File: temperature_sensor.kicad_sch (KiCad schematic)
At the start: 13 parts, among them U3 XIAO-SAMD21-SMD, U5 TMP37FT9Z

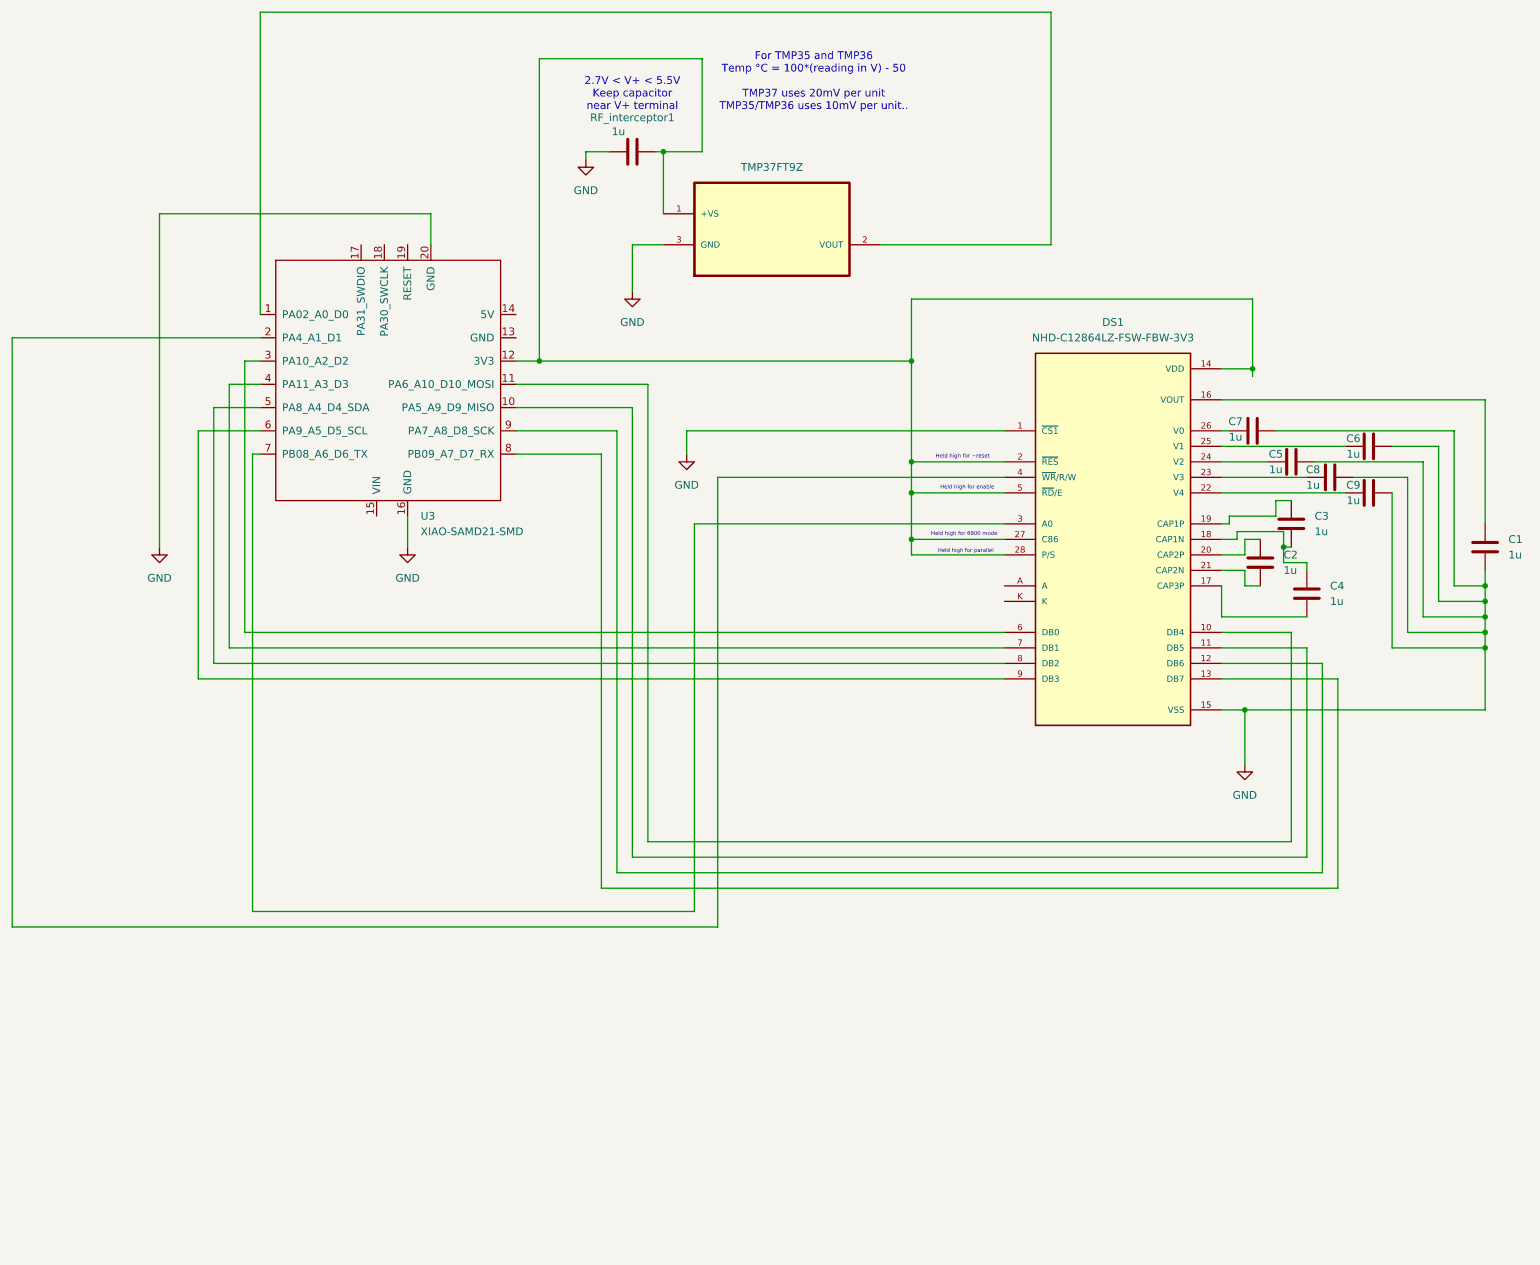
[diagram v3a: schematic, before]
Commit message: added potentiometer, photoresistor, switch between the two and off, and added a F/C switch. need to up current into LCD's A pin
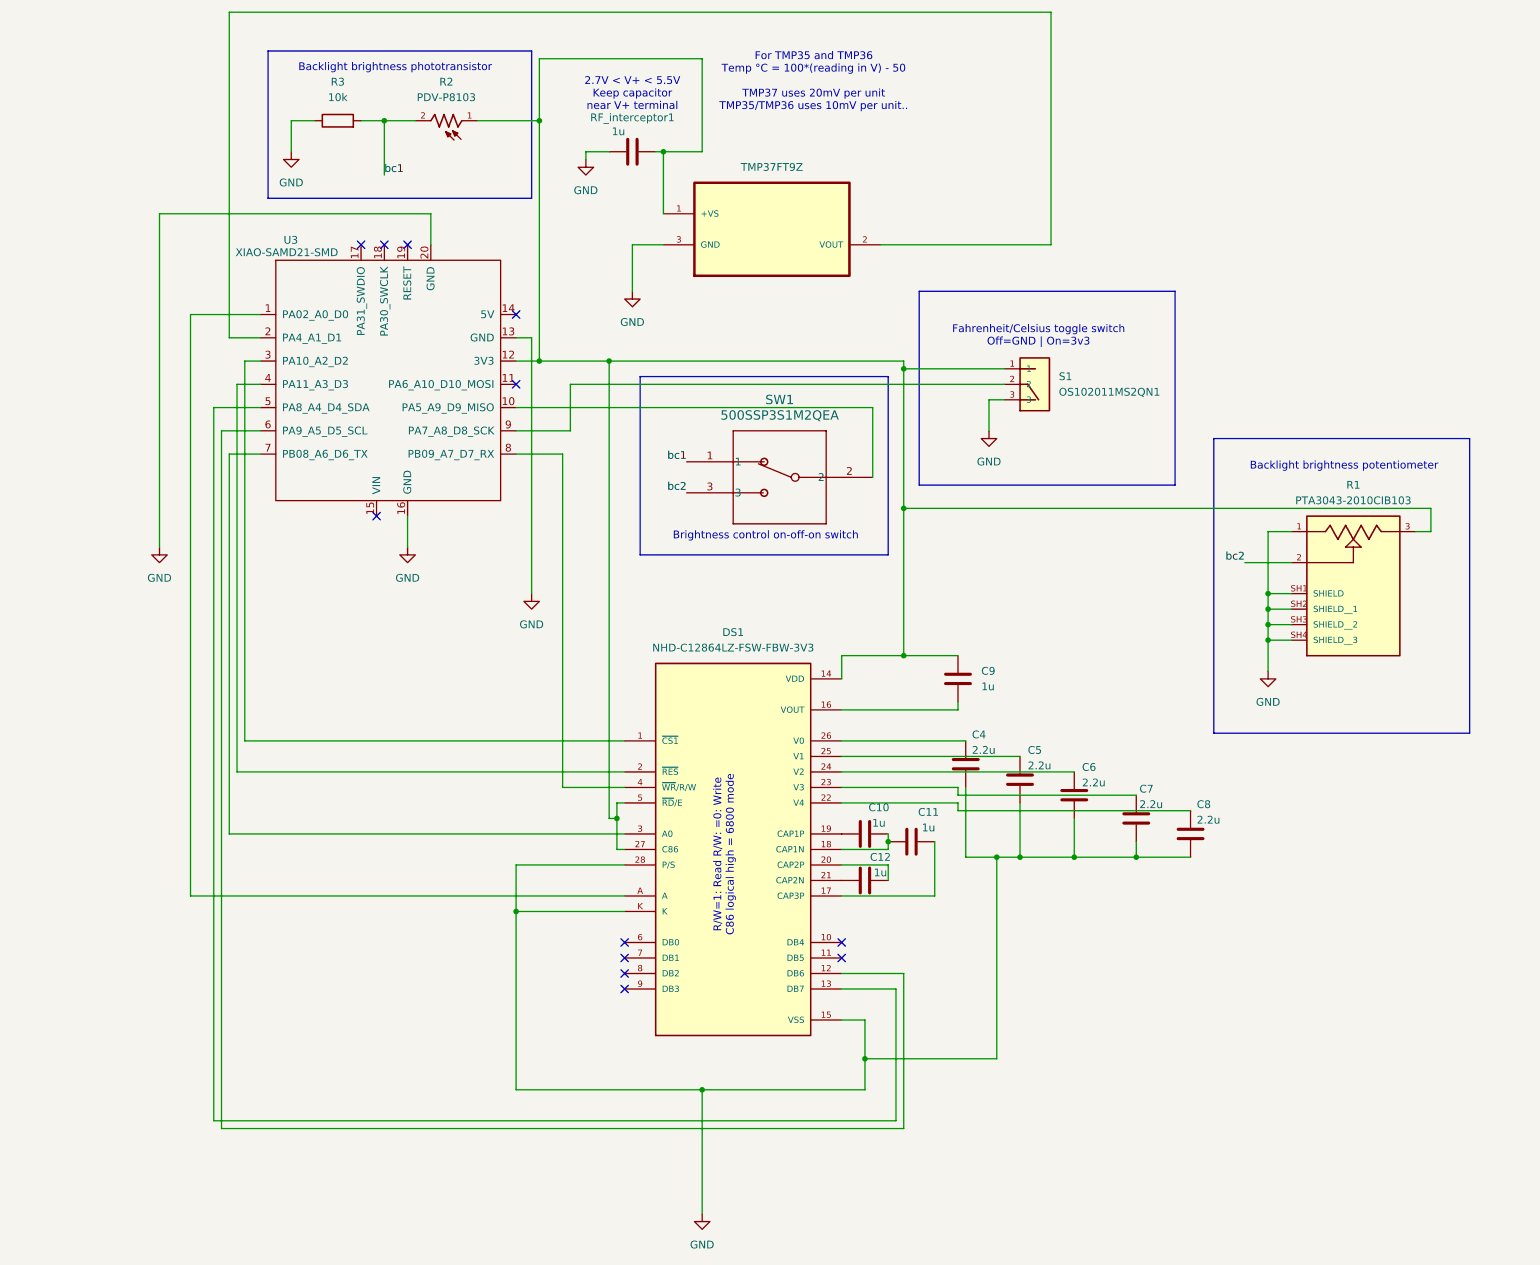
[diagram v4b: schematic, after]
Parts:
- removed C1, C2, C3: 1u, symbol Device:C
- added C10, C11, C12: 1u, symbol Device:C
- added R1: PTA3043-2010CIB103, PTA3043-2010CIB103:TRIM_PTA3043-2010CIB103, symbol PTA3043-2010CIB103:PTA3043-2010CIB103
- added R2: PDV-P8103, PDV-P8103:PHODET_PDV-P8103, symbol PDV-P8103:PDV-P8103
- added R3: 10k, symbol Device:R
- added S1: OS102011MS2QN1, OS102011MS2QN1:SW_OS102011MS2QN1, symbol OS102011MS2QN1:OS102011MS2QN1
- added SW1: 500SSP3S1M2QEA, TO_1M2QEA_EWI, symbol OnOffOn500SSP3S1M2QEA:500SSP3S1M2QEA
- C4, C5, C6, C7, C8: value 1u -> 2.2u
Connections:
- net GND: now also C4.1, C5.1, C6.1, C7.1, C8.1, DS1.28 (P/S), DS1.K, U3.13 (GND), R1.1, R1.SH1 (SHIELD), R1.SH2 (SHIELD__1), R1.SH3 (SHIELD__2), R1.SH4 (SHIELD__3), R3.1, S1.3; no longer C5.2, C6.2, C7.2, C8.2, C9.2, DS1.1 (~{CS1})
- net at C9.1: now also DS1.16 (VOUT); no longer DS1.22 (V4)
- net at DS1.26 (V0): now also C4.2; no longer C7.1
- net at DS1.14 (VDD), DS1.27 (C86), DS1.5 (~{RD}/E)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: now also C9.2, R1.3, R2.1, S1.1; no longer DS1.2 (~{RES}), DS1.28 (P/S)
- net at DS1.20 (CAP2P): now also C12.2
- net at DS1.21 (CAP2N): now also C12.1
- net at DS1.10 (DB4): no longer U3.11 (PA6_A10_D10_MOSI)
- net at U3.10 (PA5_A9_D9_MISO): now also SW1.2; no longer DS1.11 (DB5)
- net at DS1.12 (DB6): now also U3.6 (PA9_A5_D5_SCL); no longer U3.9 (PA7_A8_D8_SCK)
- net at DS1.13 (DB7): now also U3.5 (PA8_A4_D4_SDA); no longer U3.8 (PB09_A7_D7_RX)
- net at DS1.17 (CAP3P): now also C11.2; no longer C4.2
- net at DS1.18 (CAP1N): now also C10.2, C11.1; no longer C4.1
- net at DS1.19 (CAP1P): now also C10.1
- net at DS1.23 (V3): now also C7.2; no longer C8.1
- net at DS1.24 (V2): now also C6.2; no longer C5.1
- net at DS1.25 (V1): now also C5.2; no longer C6.1
- net at DS1.4 (~{WR}/R/W): now also U3.8 (PB09_A7_D7_RX); no longer U3.2 (PA4_A1_D1)
- net at U3.3 (PA10_A2_D2): now also DS1.1 (~{CS1}); no longer DS1.6 (DB0)
- net at U3.4 (PA11_A3_D3): now also DS1.2 (~{RES}); no longer DS1.7 (DB1)
- net at DS1.8 (DB2): no longer U3.5 (PA8_A4_D4_SDA)
- net at DS1.9 (DB3): no longer U3.6 (PA9_A5_D5_SCL)
- net at DS1.A: now also U3.1 (PA02_A0_D0)
- net at U5.2 (VOUT): now also U3.2 (PA4_A1_D1); no longer U3.1 (PA02_A0_D0)
- new net: C8.2, DS1.22 (V4)
- new net: S1.2, U3.9 (PA7_A8_D8_SCK)
- new net bc1: R2.2, R3.2, SW1.1
- new net bc2: R1.2, SW1.3
- no-connect marks 0 -> 12
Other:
- note added: "Backlight brightness phototransistor"
- note added: "Backlight brightness potentiometer"
- note added: "Brightness control on-off-on switch"
- note added: "Fahrenheit/Celsius toggle switch Off=GND | On=3v3"
- note added: "R/W=1: Read R/W: =0: Write C86 logical high = 6800 mode"
- note removed: "Held high for 6800 mode"
- note removed: "Held high for enable"
- note removed: "Held high for parallel"
- note removed: "Held high for ~reset"
- moved on the sheet: DS1

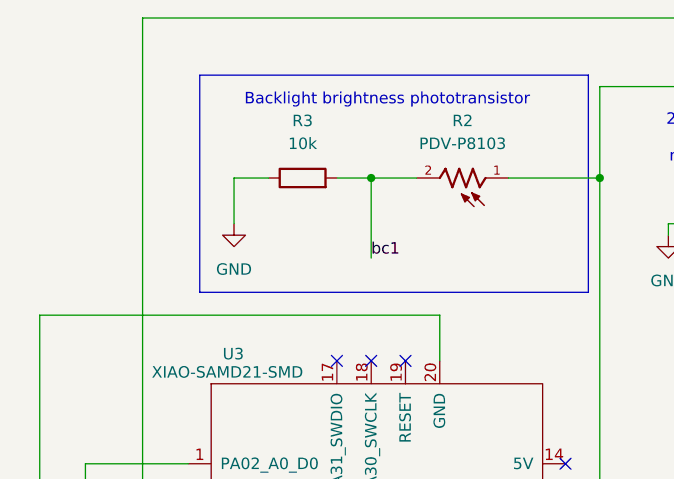
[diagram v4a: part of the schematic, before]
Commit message: got everything except the MOSFET to step up the current to 80mA.  all footprints added
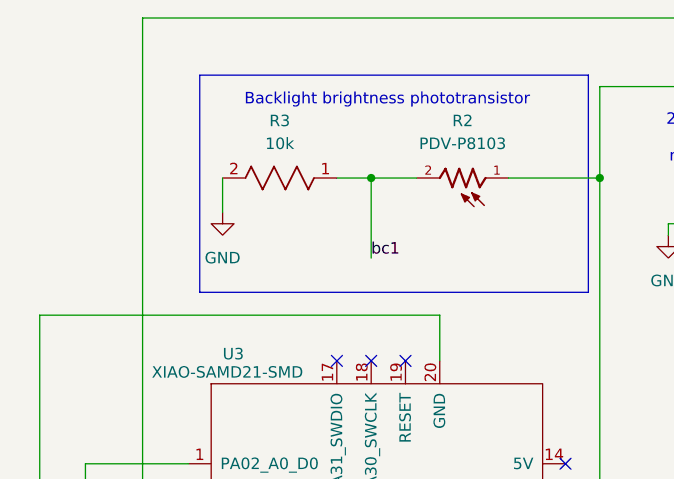
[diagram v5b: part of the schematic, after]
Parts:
- C10, C11, C12, C4, C5, C6, C7, C8, C9: footprint (none) -> Capacitor_SMD:C_0603_1608Metric_Pad1.08x0.95mm_HandSolder
- DS1: footprint NHD-C12864LZ-FSW-FBW-3V3:LCD_NHD-C12864LZ-FSW-FBW-3V3 -> 1_my_custom_library:LCD_NHD-C12864LZ-FSW-FBW-3V3
- R1: footprint PTA3043-2010CIB103:TRIM_PTA3043-2010CIB103 -> 1_my_custom_library:slide_potentiometer
- R2: footprint PDV-P8103:PHODET_PDV-P8103 -> 1_my_custom_library:photoresistor
- R3: footprint (none) -> 1_my_custom_library:YAG_MF25_YAG; symbol Device:R -> 10kresistor:MFR-25FRF52-10K
- RF_interceptor1: footprint Capacitor_SMD:C_1210_3225Metric_Pad1.33x2.70mm_HandSolder -> Capacitor_SMD:C_0603_1608Metric_Pad1.08x0.95mm_HandSolder
- S1: footprint OS102011MS2QN1:SW_OS102011MS2QN1 -> 1_my_custom_library:slideSwitch
- SW1: footprint TO_1M2QEA_EWI -> 1_my_custom_library:onOffOn
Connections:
- net GND: now also R3.2; no longer R3.1
- net bc1: now also R3.1; no longer R3.2
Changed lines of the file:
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@@
 	(wire
 		(pts
-			(xy 63.5 83.82) (xy 63.5 78.74)
-		)
-		(stroke
-			(width 0)
-			(type default)
-		)
-	)
-	(wire
-		(pts
 			(xy 161.29 198.12) (xy 161.29 196.85)
 		)
@@
 	(wire
 		(pts
-			(xy 63.5 78.74) (xy 67.31 78.74)
-		)
-		(stroke
-			(width 0)
-			(type default)
-		)
-	)
-	(wire
-		(pts
 			(xy 191.77 193.04) (xy 191.77 199.39)
 		)
@@
 	(wire
 		(pts
+			(xy 62.23 82.55) (xy 62.23 78.74)
+		)
+		(stroke
+			(width 0)
+			(type default)
+		)
+	)
+	(wire
+		(pts
 			(xy 210.82 199.39) (xy 201.93 199.39)
 		)
@@
 			)
 		)
-		(property "Footprint" "TO_1M2QEA_EWI"
+		(property "Footprint" "1_my_custom_library:onOffOn"
 			(at 128.27 134.62 0)
 			(effects
@@
 			)
 		)
-		(property "Footprint" "Capacitor_SMD:C_1210_3225Metric_Pad1.33x2.70mm_HandSolder"
+		(property "Footprint" "Capacitor_SMD:C_0603_1608Metric_Pad1.08x0.95mm_HandSolder"
 			(at 123.19 82.8548 0)
 			(effects
@@
 			)
 		)
-		(property "Footprint" ""
+		(property "Footprint" "Capacitor_SMD:C_0603_1608Metric_Pad1.08x0.95mm_HandSolder"
 			(at 168.91 195.8848 0)
 			(effects
@@
 			)
 		)
-		(property "Footprint" ""
+		(property "Footprint" "Capacitor_SMD:C_0603_1608Metric_Pad1.08x0.95mm_HandSolder"
 			(at 173.0248 180.34 0)
 			(effects
@@
 			)
 		)
-		(property "Footprint" "NHD-C12864LZ-FSW-FBW-3V3:LCD_NHD-C12864LZ-FSW-FBW-3V3"
+		(property "Footprint" "1_my_custom_library:LCD_NHD-C12864LZ-FSW-FBW-3V3"
 			(at 135.89 195.58 0)
 			(effects
@@
 	(symbol
 		(lib_id "power:GND")
-		(at 119.38 106.68 0)
+		(at 62.23 82.55 0)
 		(unit 1)
 		(exclude_from_sim no)
@@
 		(dnp no)
 		(fields_autoplaced yes)
-		(property "Reference" "#PWR03"
-			(at 119.38 113.03 0)
+		(property "Reference" "#PWR06"
+			(at 62.23 88.9 0)
 			(effects
 				(font
@@
 		)
 		(property "Value" "GND"
-			(at 119.38 111.76 0)
+			(at 62.23 87.63 0)
 			(effects
 				(font
@@
 		)
 		(property "Footprint" ""
-			(at 119.38 106.68 0)
+			(at 62.23 82.55 0)
 			(effects
 				(font
@@
 		)
 		(property "Datasheet" ""
-			(at 119.38 106.68 0)
+			(at 62.23 82.55 0)
 			(effects
 				(font
@@
 		)
 		(property "Description" "Power symbol creates a global label with name \"GND\" , ground"
-			(at 119.38 106.68 0)
+			(at 62.23 82.55 0)
 			(effects
 				(font
@@
 		)
 		(instances
-			(project "temperature_sensor"
+			(project ""
 				(path "/81d443e3-ba1c-446b-9993-4a57d2542686"
-					(reference "#PWR03")
+					(reference "#PWR06")
 					(unit 1)
 				)
@@
 	(symbol
 		(lib_id "power:GND")
-		(at 63.5 83.82 0)
+		(at 119.38 106.68 0)
 		(unit 1)
 		(exclude_from_sim no)
@@
 		(dnp no)
 		(fields_autoplaced yes)
-		(property "Reference" "#PWR06"
-			(at 63.5 90.17 0)
+		(property "Reference" "#PWR03"
+			(at 119.38 113.03 0)
 			(effects
 				(font
@@
 		)
 		(property "Value" "GND"
-			(at 63.5 88.9 0)
+			(at 119.38 111.76 0)
 			(effects
 				(font
@@
 		)
 		(property "Footprint" ""
-			(at 63.5 83.82 0)
+			(at 119.38 106.68 0)
 			(effects
 				(font
@@
 		)
 		(property "Datasheet" ""
-			(at 63.5 83.82 0)
+			(at 119.38 106.68 0)
 			(effects
 				(font
@@
 		)
 		(property "Description" "Power symbol creates a global label with name \"GND\" , ground"
-			(at 63.5 83.82 0)
+			(at 119.38 106.68 0)
 			(effects
 				(font
@@
 		)
 		(instances
-			(project ""
+			(project "temperature_sensor"
 				(path "/81d443e3-ba1c-446b-9993-4a57d2542686"
-					(reference "#PWR06")
+					(reference "#PWR03")
 					(unit 1)
 				)
@@
 	)
 	(symbol
-		(lib_id "Device:R")
-		(at 71.12 78.74 90)
+		(lib_id "10kresistor:MFR-25FRF52-10K")
+		(at 74.93 78.74 180)
 		(unit 1)
 		(exclude_from_sim no)
@@
 		(fields_autoplaced yes)
 		(property "Reference" "R3"
-			(at 71.12 72.39 90)
+			(at 68.58 72.39 0)
 			(effects
 				(font
@@
 		)
 		(property "Value" "10k"
-			(at 71.12 74.93 90)
+			(at 68.58 74.93 0)
 			(effects
 				(font
@@
 			)
 		)
-		(property "Footprint" ""
-			(at 71.12 80.518 90)
+		(property "Footprint" "1_my_custom_library:YAG_MF25_YAG"
+			(at 74.93 78.74 0)
 			(effects
 				(font
 					(size 1.27 1.27)
+					(italic yes)
 				)
 				(hide yes)
 			)
 		)
-		(property "Datasheet" "~"
-			(at 71.12 78.74 0)
+		(property "Datasheet" "MFR-25FRF52-10K"
+			(at 74.93 78.74 0)
 			(effects
 				(font
 					(size 1.27 1.27)
+					(italic yes)
 				)
 				(hide yes)
@@
 		)
 		(property "Description" "Resistor"
-			(at 71.12 78.74 0)
+			(at 74.93 78.74 0)
 			(effects
 				(font
@@
 			)
 		)
-		(property "Footprint" "OS102011MS2QN1:SW_OS102011MS2QN1"
+		(property "Footprint" "1_my_custom_library:slideSwitch"
 			(at 185.42 121.92 0)
 			(effects
@@
 			)
 		)
-		(property "Footprint" "PTA3043-2010CIB103:TRIM_PTA3043-2010CIB103"
+		(property "Footprint" "1_my_custom_library:slide_potentiometer"
 			(at 237.49 151.13 0)
 			(effects
@@
 			)
 		)
-		(property "Footprint" ""
+		(property "Footprint" "Capacitor_SMD:C_0603_1608Metric_Pad1.08x0.95mm_HandSolder"
 			(at 161.29 202.2348 0)
 			(effects
@@
 			)
 		)
-		(property "Footprint" ""
+		(property "Footprint" "Capacitor_SMD:C_0603_1608Metric_Pad1.08x0.95mm_HandSolder"
 			(at 190.8048 185.42 0)
 			(effects
@@
 			)
 		)
-		(property "Footprint" ""
+		(property "Footprint" "Capacitor_SMD:C_0603_1608Metric_Pad1.08x0.95mm_HandSolder"
 			(at 171.7548 166.37 0)
 			(effects
@@
 			)
 		)
-		(property "Footprint" ""
+		(property "Footprint" "Capacitor_SMD:C_0603_1608Metric_Pad1.08x0.95mm_HandSolder"
 			(at 200.9648 189.23 0)
 			(effects
@@
 			)
 		)
-		(property "Footprint" "PDV-P8103:PHODET_PDV-P8103"
+		(property "Footprint" "1_my_custom_library:photoresistor"
 			(at 88.9 78.74 0)
 			(effects
@@
 			)
 		)
-		(property "Footprint" ""
+		(property "Footprint" "Capacitor_SMD:C_0603_1608Metric_Pad1.08x0.95mm_HandSolder"
 			(at 209.8548 191.77 0)
 			(effects
@@
 			)
 		)
-		(property "Footprint" ""
+		(property "Footprint" "Capacitor_SMD:C_0603_1608Metric_Pad1.08x0.95mm_HandSolder"
 			(at 181.9148 182.88 0)
 			(effects
@@
 			)
 		)
-		(property "Footprint" ""
+		(property "Footprint" "Capacitor_SMD:C_0603_1608Metric_Pad1.08x0.95mm_HandSolder"
 			(at 161.29 194.6148 0)
 			(effects

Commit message: this should be good to ship but i want to add some LEDs and some test points
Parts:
- added R4: 820, Resistor_SMD:R_1206_3216Metric_Pad1.30x1.75mm_HandSolder, symbol Device:R
- added U1: MMBT3904LT1G, SOT-23_3L_ONS, symbol bjt:MMBT3904LT1G
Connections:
- net GND: now also U1.2 (EMITTER); no longer DS1.K
- net at C9.2, DS1.14 (VDD), DS1.27 (C86)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: now also DS1.A
- net at U3.1 (PA02_A0_D0): now also R4.1; no longer DS1.A
- new net: DS1.K, U1.3 (COLLECTOR)
- new net: R4.2, U1.1 (BASE)

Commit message: ready for PCB design
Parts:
- added TP1: gnd_TP, Connector_Pin:Pin_D1.0mm_L10.0mm, symbol Connector:TestPoint
- added TP2: pot_TP, Connector_Pin:Pin_D1.0mm_L10.0mm, symbol Connector:TestPoint
- added TP3: photoresistor_TP, Connector_Pin:Pin_D1.0mm_L10.0mm, symbol Connector:TestPoint
- added TP4: PWM_TP, Connector_Pin:Pin_D1.0mm_L10.0mm, symbol Connector:TestPoint
- added TP5: K_TP, Connector_Pin:Pin_D1.0mm_L10.0mm, symbol Connector:TestPoint
- added TP6: SCL_TP, Connector_Pin:Pin_D1.0mm_L10.0mm, symbol Connector:TestPoint
- added TP7: SI_TP, Connector_Pin:Pin_D1.0mm_L10.0mm, symbol Connector:TestPoint
- added TP8: fahrenheit_celsius_TP, Connector_Pin:Pin_D1.0mm_L10.0mm, symbol Connector:TestPoint
- added TP9: 3v3_TP, Connector_Pin:Pin_D1.0mm_L10.0mm, symbol Connector:TestPoint
- R4: footprint Resistor_SMD:R_1206_3216Metric_Pad1.30x1.75mm_HandSolder -> CRGP2512F820R:RESC6332X65N; symbol Device:R -> CRGP2512F820R:CRGP2512F820R
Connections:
- net GND: now also TP1.1
- net bc1: now also TP3.1
- net bc2: now also TP2.1
- net at C9.2, DS1.14 (VDD), DS1.27 (C86)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: now also TP9.1
- net at DS1.12 (DB6), U3.6 (PA9_A5_D5_SCL): now also TP6.1
- net at DS1.13 (DB7), U3.5 (PA8_A4_D4_SDA): now also TP7.1
- net at DS1.K, U1.3 (COLLECTOR): now also TP5.1
- net at S1.2, U3.9 (PA7_A8_D8_SCK): now also TP8.1
- net at R4.2, U1.1 (BASE): now also TP4.1

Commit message: initial pcb design
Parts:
- R4: footprint CRGP2512F820R:RESC6332X65N -> 1_my_custom_library:RESC6332X65N
- U1: footprint SOT-23_3L_ONS -> 1_my_custom_library:SOT-23_3L_ONS
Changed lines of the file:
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@@
 			)
 		)
-		(property "Footprint" "CRGP2512F820R:RESC6332X65N"
+		(property "Footprint" "1_my_custom_library:RESC6332X65N"
 			(at 49.53 262.89 0)
 			(effects
@@
 			)
 		)
-		(property "Footprint" "SOT-23_3L_ONS"
+		(property "Footprint" "1_my_custom_library:SOT-23_3L_ONS"
 			(at 58.42 252.73 0)
 			(effects
